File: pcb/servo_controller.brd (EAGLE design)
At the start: 68.6 x 53.3 mm, 49 parts, among them IC1 PIC18F452, IC2 LM2936MP-3.0, Q1 10Mhz, U1 ARDUINOR3-DIMENSION

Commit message: Leg sensor + elec
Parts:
- RSENSE: value (none) -> 0.1
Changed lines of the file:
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@@
 <attribute name="VALUE" x="18.256596875" y="9.748525" size="1.016" layer="27" rot="R45"/>
 </element>
-<element name="RSENSE" library="rcl" package="R4527" value="" x="18.415" y="23.1775" smashed="yes" rot="R270">
+<element name="RSENSE" library="rcl" package="R4527" value="0.1" x="18.415" y="23.1775" smashed="yes" rot="R270">
 <attribute name="NAME" x="14.9225" y="30.1625" size="1.27" layer="25"/>
 <attribute name="VALUE" x="13.335" y="28.8925" size="1.27" layer="27" rot="R270"/>

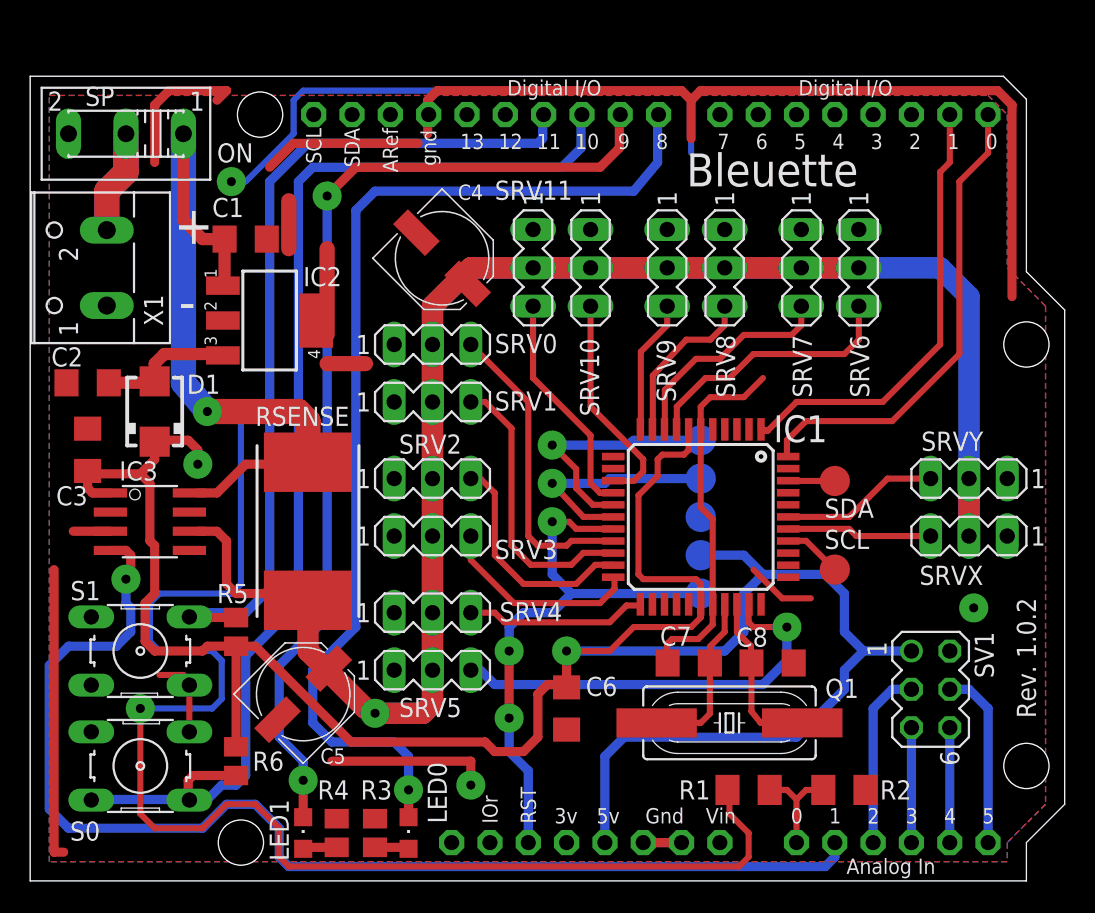
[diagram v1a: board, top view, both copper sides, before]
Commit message: Rev 1.1.0
- Added zener in analog paths (current / voltage)
- C2 and C3 inversed
- Gnd and Vss connected
- Added resistor (R7) to RA4 (open collector)
- Rsense value to 0.02Ω
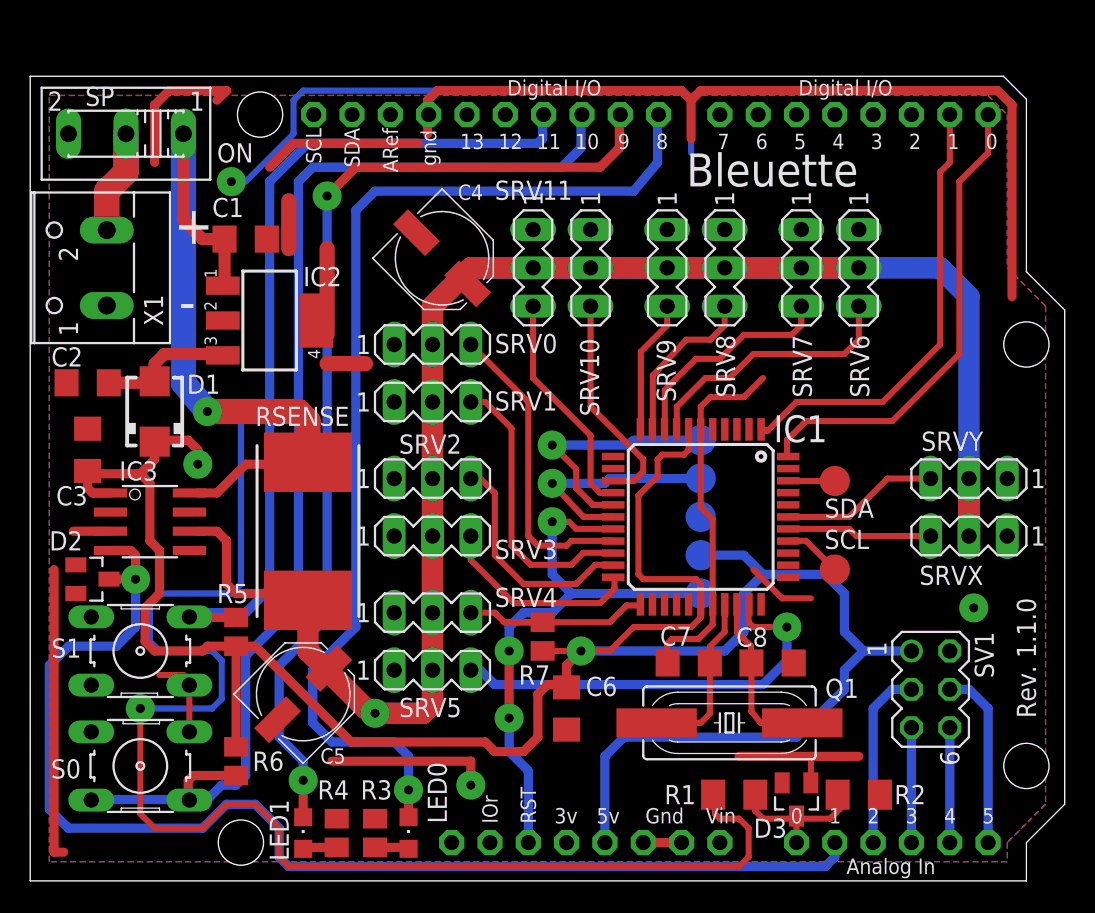
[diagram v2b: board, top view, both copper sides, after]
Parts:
- added D2, D3: 5v1, diode:SOT23
- added R7: 2.2k, rcl:M0805
- RSENSE: value 0.1 -> 0.02
- moved R1 1.00 mm to (46.7, 5.71)
- moved R2 1.00 mm to (54.9, 5.71)
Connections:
- removed net GND: U1.GND1, U1.GND2
- net +5V: now also R7.2
- net LIPO_VOLTAGE: now also D3.3
- net N$5: now also R7.1
- net SERVO_CURRENT: now also D2.3
- net VSS: now also D2.1, D3.1, U1.GND1, U1.GND2
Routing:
- net VSS: track 193.2 -> 208.0 mm
- net GND: track 5.08 -> 0.00 mm
- net LIPO_VOLTAGE: track 6.93 -> 10.7 mm
- net N$5: track 12.0 -> 14.5 mm
- net SERVO_CURRENT: track 80.0 -> 81.9 mm
- net +5V: track 159.1 -> 160.4 mm
- net VEE: track 171.4 -> 170.4 mm
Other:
- board text added: "Rev. 1.1.0"
- board text removed: "Rev. 1.0.2"

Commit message: Rev 1.2.0
- Added C9 for better 5V filter
- Added reset jumper
- Added OpenHardware logo
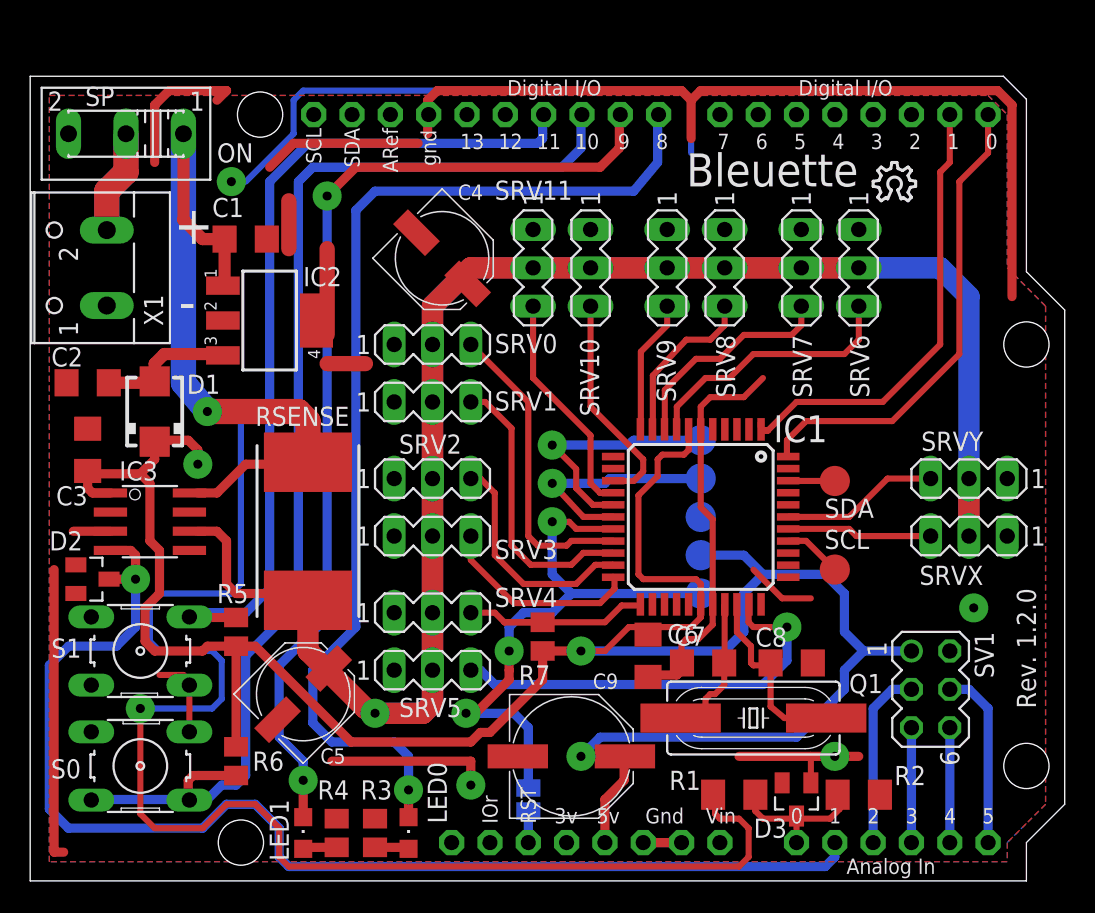
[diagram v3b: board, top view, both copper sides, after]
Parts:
- added C9: (no value), rcl:PANASONIC_F
- added SJ1: (no value), jumper:SJ
- added U$1: (no value), ohw-logo:OSHW_8X100_NOTEXT
- moved C6 6.43 mm to (41.0, 14.9)
- moved Q1 1.62 mm to (47.9, 10.8)
- moved C8 1.27 mm to (50.5, 14.4)
- moved C7 0.95 mm to (44.6, 14.4)
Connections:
- new net N$16: SJ1.2, U1.RESET
- net +5V: now also C9.+
- net UC_RESET: now also SJ1.1; no longer U1.RESET
- net VSS: now also C9.-
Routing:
- net +5V: track 160.4 -> 162.9 mm, vias 2 -> 3
- net N$16: track 0.00 -> 2.10 mm
- net VSS: track 208.0 -> 209.9 mm, vias 3 -> 4
- net N$25: track 11.2 -> 12.5 mm
- net UC_RESET: track 38.0 -> 38.9 mm
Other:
- board text added: "Rev. 1.2.0"
- board text removed: "Rev. 1.1.0"

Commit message: Rev. 1.2.1
- Change switch to 2.54mm one
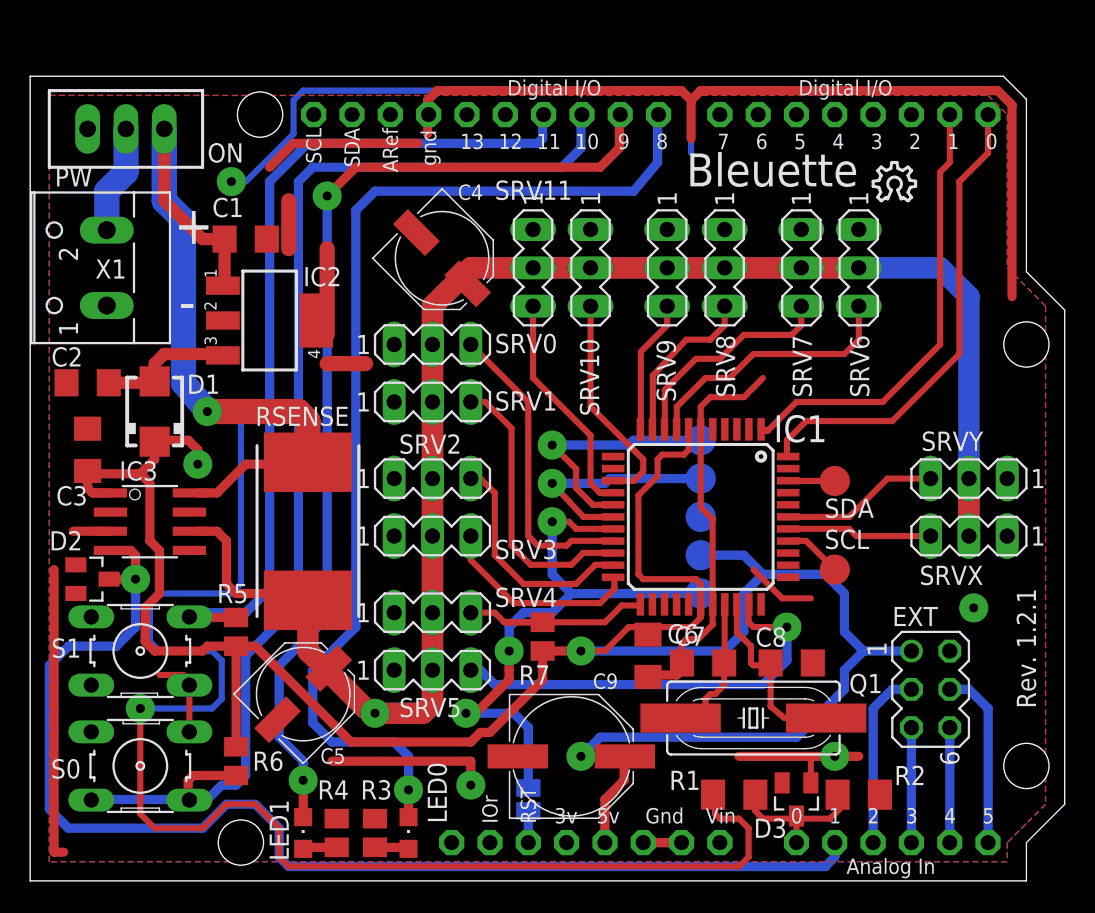
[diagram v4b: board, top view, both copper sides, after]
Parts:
- removed SP: (no value), switch:255SB
- added PW: TL36PO, switch:TL3XPO
- renumbered SV1 to EXT
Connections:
- net N$15: now also PW.2; no longer SP.2
- net VDD: now also PW.1; no longer SP.1
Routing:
- net VSS: track 209.9 -> 200.0 mm
- net N$15: track 13.8 -> 7.23 mm
- net VDD: track 142.4 -> 144.1 mm
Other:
- board text added: "Rev. 1.2.1"
- board text removed: "Rev. 1.2.0"
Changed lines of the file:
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@@
 <hole x="13.97" y="2.54" drill="3"/>
 <hole x="15.24" y="50.8" drill="3"/>
-<text x="12.3825" y="47.625" size="1.27" layer="25">ON</text>
+<text x="11.7475" y="47.625" size="1.27" layer="25">ON</text>
 <text x="43.4975" y="46.0375" size="2.1844" layer="25">Bleuette</text>
 <text x="54.61" y="33.9725" size="2.1844" layer="26" rot="MR0">Bleuette</text>
@@
 <text x="9.525" y="42.2275" size="2.54" layer="25">+</text>
 <text x="9.8425" y="37.1475" size="2.54" layer="25">-</text>
-<text x="66.675" y="11.43" size="1.27" layer="25" rot="R90">Rev. 1.2.0</text>
+<text x="66.675" y="11.43" size="1.27" layer="25" rot="R90">Rev. 1.2.1</text>
 </plain>
 <attributes>
@@
 <attribute name="VALUE" x="56.1975" y="8.255" size="1.27" layer="27" rot="R180"/>
 </element>
-<element name="SP" library="switch" package="255SB" value="" x="6.35" y="49.53" smashed="yes" rot="R180">
-<attribute name="NAME" x="5.588" y="52.6415" size="1.27" layer="25" ratio="10" rot="R180"/>
-<attribute name="VALUE" x="6.35" y="45.974" size="1.27" layer="27" ratio="10" rot="R180"/>
-</element>
 <element name="S0" library="switch-omron" package="B3F-10XX" value="" x="7.3025" y="7.62" smashed="yes" rot="R180">
 <attribute name="OC_NEWARK" value="36M3542" x="7.3025" y="7.62" size="1.778" layer="27" rot="R180" display="off"/>
@@
 <attribute name="VALUE" x="6.223" y="27.305" size="1.27" layer="27" rot="R90"/>
 </element>
-<element name="SV1" library="con-lstb" package="MA03-2" value="" x="59.69" y="12.7" rot="R270">
+<element name="EXT" library="con-lstb" package="MA03-2" value="" x="59.69" y="12.7" smashed="yes" rot="R270">
 <attribute name="OC_NEWARK" value="unknown" x="59.69" y="12.7" size="1.778" layer="27" rot="R270" display="off"/>
 <attribute name="MPN" value="" x="59.69" y="12.7" size="1.778" layer="27" rot="R270" display="off"/>
 <attribute name="MF" value="" x="59.69" y="12.7" size="1.778" layer="27" rot="R270" display="off"/>
 <attribute name="OC_FARNELL" value="unknown" x="59.69" y="12.7" size="1.778" layer="27" rot="R270" display="off"/>
+<attribute name="NAME" x="57.15" y="16.891" size="1.27" layer="25" ratio="10"/>
+<attribute name="VALUE" x="55.499" y="13.97" size="1.27" layer="27" ratio="10" rot="R270"/>
 </element>
 <element name="C5" library="rcl" package="PANASONIC_D" value="" x="18.0975" y="12.3825" smashed="yes" rot="R45">
@@
 <attribute name="VALUE" x="24.671025" y="41.1159" size="1.016" layer="27" rot="R315"/>
 </element>
-<element name="X1" library="con-wago-500" package="W237-102" value="" x="3.81" y="40.64" rot="R90">
+<element name="X1" library="con-wago-500" package="W237-102" value="" x="3.81" y="40.64" smashed="yes" rot="R90">
 <attribute name="OC_NEWARK" value="70K9898" x="3.81" y="40.64" size="1.778" layer="27" rot="R90" display="off"/>
 <attribute name="MPN" value="237-102" x="3.81" y="40.64" size="1.778" layer="27" rot="R90" display="off"/>
 <attribute name="MF" value="" x="3.81" y="40.64" size="1.778" layer="27" rot="R90" display="off"/>
 <attribute name="OC_FARNELL" value="unknown" x="3.81" y="40.64" size="1.778" layer="27" rot="R90" display="off"/>
+<attribute name="VALUE" x="11.43" y="35.6" size="1.27" layer="27" ratio="10" rot="R90"/>
+<attribute name="NAME" x="6.3862" y="41.1988" size="1.27" layer="25" ratio="10" rot="R180"/>
 </element>
 <element name="IC2" library="national-semiconductor" package="SOT223" value="LM2936MP-3.0" x="15.875" y="37.1475" smashed="yes" rot="R270">
@@
 </element>
 <element name="U$1" library="ohw-logo" package="OSHW_8X100_NOTEXT" value="" x="55.88" y="45.085"/>
+<element name="PW" library="switch" package="TL3XPO" value="TL36PO" x="6.35" y="49.8475" smashed="yes" rot="R180">
+<attribute name="NAME" x="4.1275" y="47.3075" size="1.27" layer="25" rot="R180"/>
+<attribute name="VALUE" x="11.43" y="54.9275" size="1.778" layer="27" rot="R180"/>
+</element>
 </elements>
 <signals>
@@
 <contactref element="C3" pad="2"/>
 <wire x1="5.3213" y1="23.1775" x2="2.8575" y2="23.1775" width="0.6096" layer="1"/>
-<contactref element="SV1" pad="2"/>
+<contactref element="EXT" pad="2"/>
 <wire x1="25.7175" y1="48.895" x2="17.4625" y2="48.895" width="0.6096" layer="1"/>
 <wire x1="17.4625" y1="48.895" x2="15.875" y2="47.3075" width="0.6096" layer="1"/>
 <wire x1="43.815" y1="49.2125" x2="43.815" y2="51.7525" width="0.6096" layer="1"/>
 <wire x1="43.815" y1="51.7525" x2="43.18" y2="52.3875" width="0.6096" layer="1"/>
-<wire x1="13.0175" y1="52.3875" x2="12.3825" y2="51.7525" width="0.6096" layer="1"/>
 <wire x1="18.0975" y1="52.3875" x2="43.18" y2="52.3875" width="0.4064" layer="16"/>
 <wire x1="43.18" y1="52.3875" x2="43.815" y2="51.7525" width="0.4064" layer="16"/>
@@
 <wire x1="8.5725" y1="13.6525" x2="10.16" y2="13.6525" width="0.4064" layer="1"/>
 <wire x1="10.16" y1="13.6525" x2="10.4775" y2="13.335" width="0.4064" layer="1"/>
-<wire x1="8.255" y1="47.625" x2="8.255" y2="51.435" width="0.6096" layer="1"/>
-<wire x1="8.255" y1="51.435" x2="9.2075" y2="52.3875" width="0.6096" layer="1"/>
-<wire x1="9.2075" y1="52.3875" x2="13.0175" y2="52.3875" width="0.6096" layer="1"/>
 <wire x1="45.24375" y1="17.93875" x2="45.24375" y2="16.98625" width="0.4064" layer="1"/>
 <wire x1="45.24375" y1="16.98625" x2="44.29125" y2="16.03375" width="0.4064" layer="1"/>
@@
 <wire x1="3.81" y1="26.035" x2="4.1275" y2="25.7175" width="0.6096" layer="1"/>
 <wire x1="4.1275" y1="25.7175" x2="5.3213" y2="25.7175" width="0.6096" layer="1"/>
-<contactref element="SV1" pad="1"/>
+<contactref element="EXT" pad="1"/>
 <wire x1="37.7825" y1="9.525" x2="50.8" y2="9.525" width="0.6096" layer="16"/>
 <wire x1="50.8" y1="9.525" x2="53.975" y2="12.7" width="0.6096" layer="16"/>
@@
 <contactref element="C1" pad="1"/>
 <contactref element="R1" pad="2"/>
-<contactref element="SP" pad="1"/>
 <contactref element="IC3" pad="8"/>
-<wire x1="10.16" y1="49.53" x2="10.16" y2="43.815" width="0.8128" layer="1"/>
-<wire x1="10.16" y1="43.815" x2="11.43" y2="42.545" width="0.8128" layer="1"/>
-<wire x1="10.16" y1="49.53" x2="10.16" y2="33.02" width="1.6764" layer="16"/>
 <wire x1="10.16" y1="33.02" x2="11.7475" y2="31.115" width="1.6764" layer="16"/>
 <via x="11.7475" y="31.115" extent="1-16" drill="0.6" diameter="1.9304"/>
@@
 <wire x1="45.4025" y1="4.445" x2="45.4025" y2="5.2675" width="0.4064" layer="1"/>
 <wire x1="45.4025" y1="5.2675" x2="45.2725" y2="5.715" width="0.4064" layer="1"/>
+<contactref element="PW" pad="1"/>
+<wire x1="10.16" y1="33.02" x2="10.16" y2="43.815" width="1.6764" layer="16"/>
+<wire x1="10.16" y1="43.815" x2="8.89" y2="45.085" width="1.6764" layer="16"/>
+<wire x1="8.89" y1="45.085" x2="8.89" y2="49.8475" width="1.6764" layer="16"/>
+<wire x1="11.43" y1="42.545" x2="8.89" y2="45.085" width="0.8128" layer="1"/>
+<wire x1="8.89" y1="45.085" x2="8.89" y2="49.8475" width="0.8128" layer="1"/>
 <wire x1="18.415" y1="27.9908" x2="18.415" y2="27.7525" width="0" layer="19" extent="1-1"/>
 </signal>
@@
 </signal>
 <signal name="OPTION0">
-<contactref element="SV1" pad="3"/>
+<contactref element="EXT" pad="3"/>
 <contactref element="U1" pad="A2"/>
 <wire x1="58.42" y1="12.7" x2="57.15" y2="12.7" width="0.6096" layer="16"/>
@@
 <signal name="OPTION2">
 <contactref element="U1" pad="A4"/>
-<contactref element="SV1" pad="6"/>
+<contactref element="EXT" pad="6"/>
 <wire x1="60.96" y1="10.16" x2="60.96" y2="2.54" width="0.6096" layer="16"/>
 </signal>
 <signal name="OPTION3">
 <contactref element="U1" pad="A5"/>
-<contactref element="SV1" pad="4"/>
+<contactref element="EXT" pad="4"/>
 <wire x1="60.96" y1="12.7" x2="62.23" y2="12.7" width="0.6096" layer="16"/>
 <wire x1="62.23" y1="12.7" x2="63.5" y2="11.43" width="0.6096" layer="16"/>
@@
 <signal name="OPTION1">
 <contactref element="U1" pad="A3"/>
-<contactref element="SV1" pad="5"/>
+<contactref element="EXT" pad="5"/>
 <wire x1="58.42" y1="10.16" x2="58.42" y2="2.54" width="0.6096" layer="16"/>
 </signal>
@@
 </signal>
 <signal name="N$15">
-<contactref element="SP" pad="2"/>
 <contactref element="X1" pad="2"/>
-<wire x1="6.35" y1="49.53" x2="6.35" y2="46.99" width="1.6764" layer="16"/>
 <wire x1="6.35" y1="46.99" x2="5.08" y2="45.72" width="1.6764" layer="16"/>
 <wire x1="5.08" y1="45.72" x2="5.08" y2="43.14" width="1.6764" layer="16"/>
-<wire x1="6.35" y1="49.53" x2="6.35" y2="46.99" width="1.6764" layer="1"/>
-<wire x1="6.35" y1="46.99" x2="5.08" y2="45.72" width="1.6764" layer="1"/>
-<wire x1="5.08" y1="45.72" x2="5.08" y2="43.18" width="1.6764" layer="1"/>
+<contactref element="PW" pad="2"/>
+<wire x1="6.35" y1="46.99" x2="6.35" y2="49.8475" width="1.6764" layer="16"/>
 </signal>
 <signal name="N$16">
@@
 </signal>
 </signals>
-<errors>
-</errors>
 </board>
 </drawing>
